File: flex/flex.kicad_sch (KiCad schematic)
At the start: 28 parts, among them J1 Conn_01x06_Female, J2 Conn_01x03_Female, J3 Conn_01x01_Female, SW1 SW_Push, SW14 SW_Push, SW19 SW_Push, SW5 SW_Push, SW9 SW_Push

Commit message: drc
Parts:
- J3: footprint Connector_PinHeader_2.54mm:PinHeader_1x01_P2.54mm_Vertical -> custom:PinHeader_1x01_P2.54mm_Vertical
- J4: renamed from J?; footprint Connector_PinHeader_2.54mm:PinHeader_1x01_P2.54mm_Vertical -> custom:PinHeader_1x01_P2.54mm_Vertical
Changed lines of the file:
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@@
   (symbol (lib_id "Connector:Conn_01x01_Female") (at 151.13 114.3 0) (unit 1)
     (in_bom yes) (on_board yes)
-    (property "Reference" "J?" (id 0) (at 151.8413 113.6078 0)
+    (property "Reference" "J4" (id 0) (at 151.8413 113.6078 0)
       (effects (font (size 1.27 1.27)) (justify left))
     )
@@
       (effects (font (size 1.27 1.27)) (justify left))
     )
-    (property "Footprint" "Connector_PinHeader_2.54mm:PinHeader_1x01_P2.54mm_Vertical" (id 2) (at 151.13 114.3 0)
+    (property "Footprint" "custom:PinHeader_1x01_P2.54mm_Vertical" (id 2) (at 151.13 114.3 0)
       (effects (font (size 1.27 1.27)) hide)
     )
@@
       (effects (font (size 1.27 1.27)) (justify left))
     )
-    (property "Footprint" "Connector_PinHeader_2.54mm:PinHeader_1x01_P2.54mm_Vertical" (id 2) (at 189.23 91.44 0)
+    (property "Footprint" "custom:PinHeader_1x01_P2.54mm_Vertical" (id 2) (at 189.23 91.44 0)
       (effects (font (size 1.27 1.27)) hide)
     )
@@
     )
     (path "/d7dd6422-5a2c-4c20-8c63-6ad26180679c"
-      (reference "J3") (unit 1) (value "Conn_01x01_Female") (footprint "Connector_PinHeader_2.54mm:PinHeader_1x01_P2.54mm_Vertical")
+      (reference "J3") (unit 1) (value "Conn_01x01_Female") (footprint "custom:PinHeader_1x01_P2.54mm_Vertical")
     )
     (path "/53891b88-f1a1-4c61-b083-3fcaa127f940"
-      (reference "J?") (unit 1) (value "Conn_01x01_Female") (footprint "Connector_PinHeader_2.54mm:PinHeader_1x01_P2.54mm_Vertical")
+      (reference "J4") (unit 1) (value "Conn_01x01_Female") (footprint "custom:PinHeader_1x01_P2.54mm_Vertical")
     )
     (path "/6254aa13-411d-4aa6-a1ef-3424dce5a979"

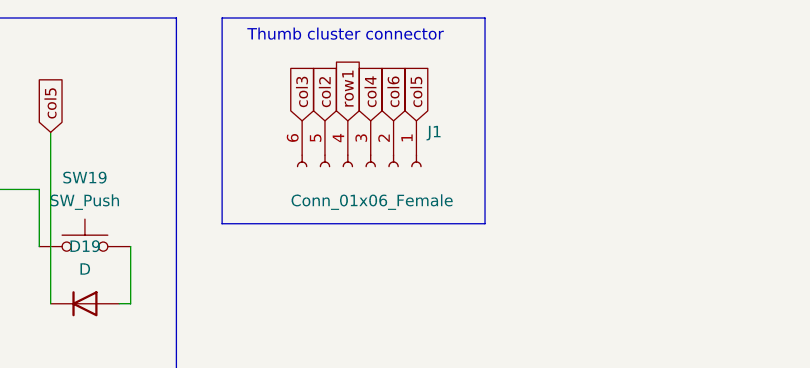
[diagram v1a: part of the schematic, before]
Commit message: flip c6 and c5
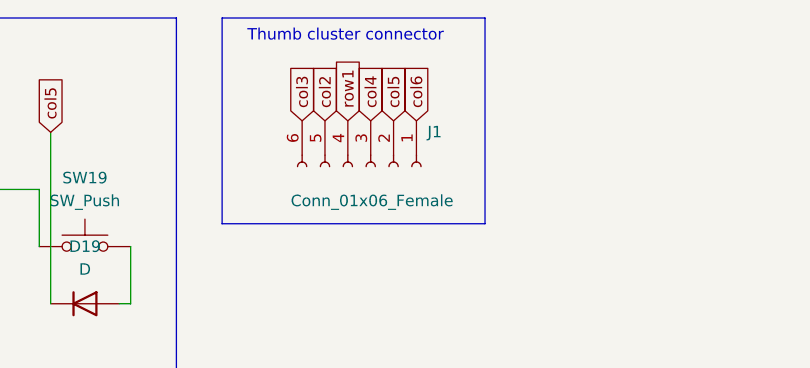
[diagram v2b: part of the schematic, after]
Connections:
- net col5: now also J1.2 (Pin_2); no longer J1.1 (Pin_1)
- net col6: now also J1.1 (Pin_1); no longer J1.2 (Pin_2)
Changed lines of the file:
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@@
     )
   )
-  (global_label "col5" (shape input) (at 153.67 30.48 90)
+  (global_label "col6" (shape input) (at 153.67 30.48 90)
     (effects (font (size 1.27 1.27)) (justify left))
     (property "Intersheet References" "${INTERSHEET_REFS}" (id 0) (at 95.25 -15.24 0)
@@
     )
   )
-  (global_label "col6" (shape input) (at 151.13 30.48 90)
+  (global_label "col5" (shape input) (at 151.13 30.48 90)
     (effects (font (size 1.27 1.27)) (justify left))
     (property "Intersheet References" "${INTERSHEET_REFS}" (id 0) (at 95.25 -15.24 0)
